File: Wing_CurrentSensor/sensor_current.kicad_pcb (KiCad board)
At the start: 2 copper layers, 50 x 50 mm, 18 parts, among them U1 TL084

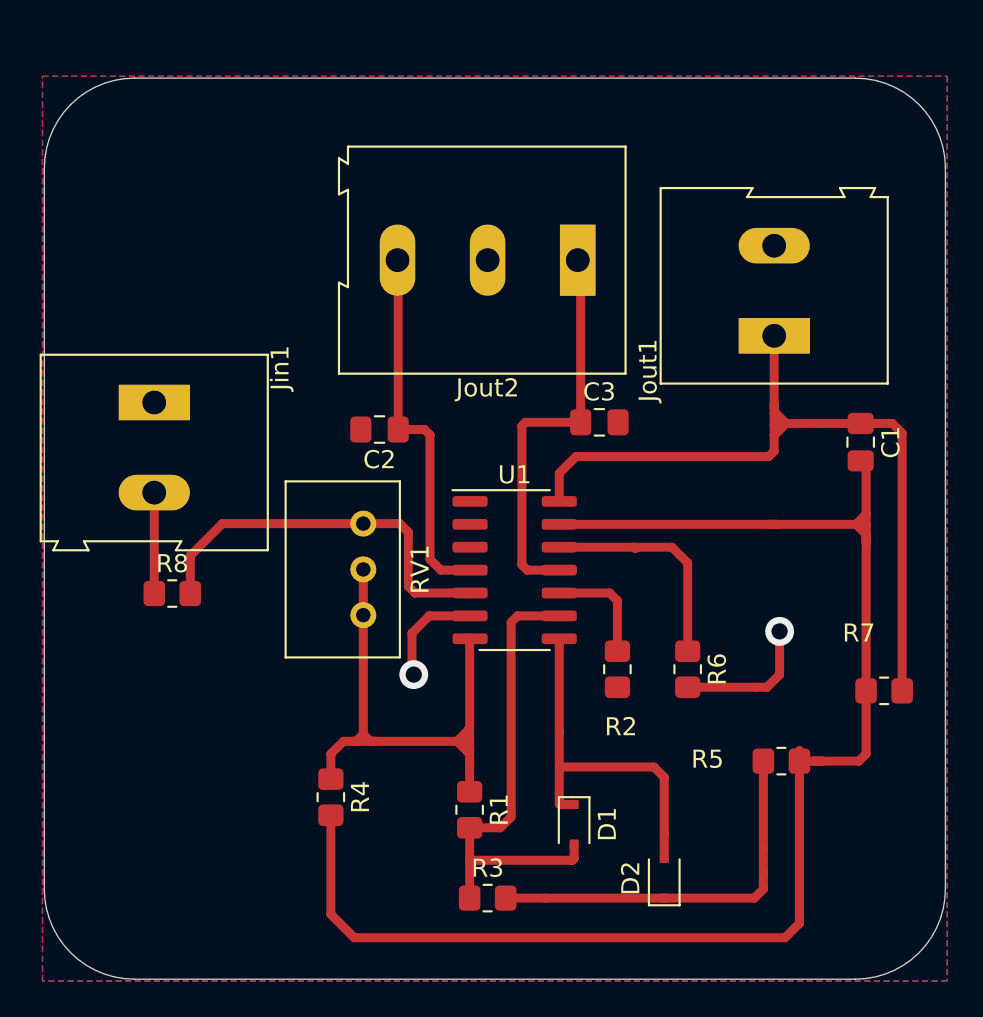
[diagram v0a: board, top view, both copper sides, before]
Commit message: Manual version
1rst version of the PCB ad8226 and TL084
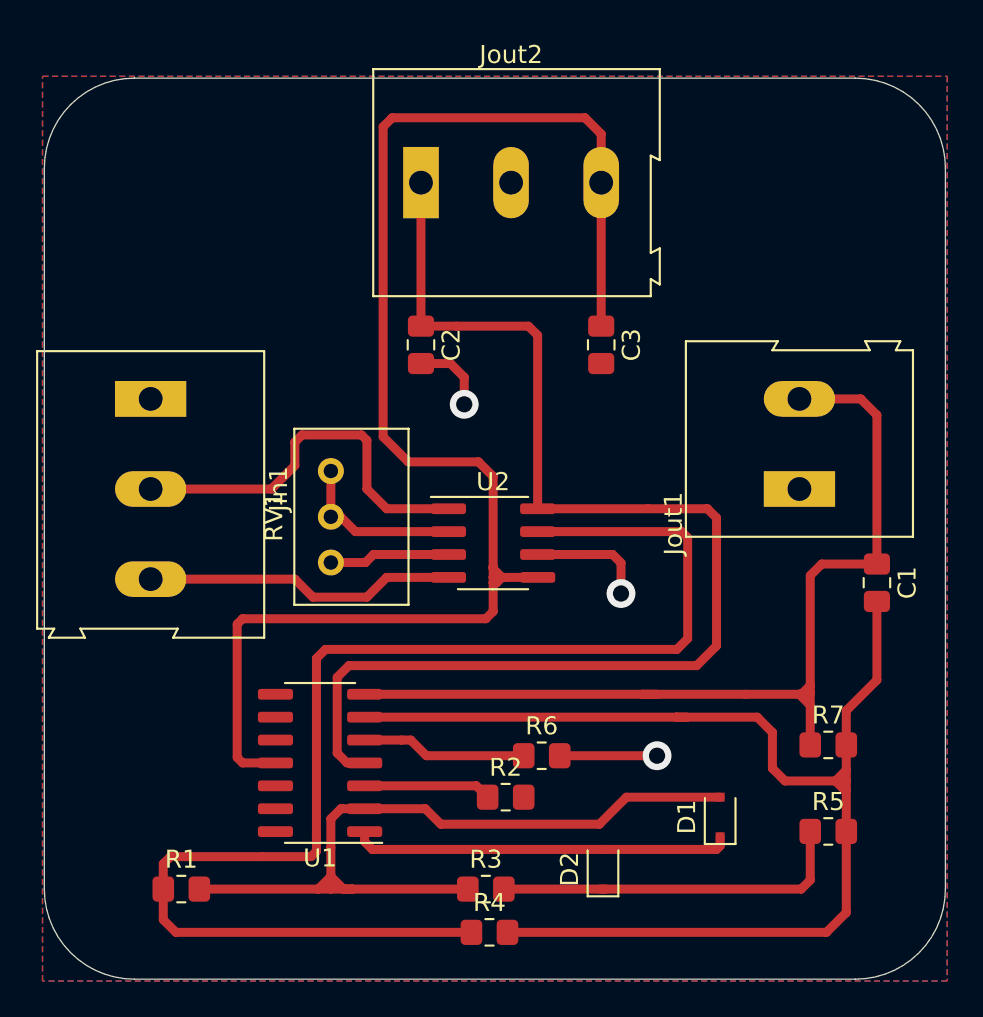
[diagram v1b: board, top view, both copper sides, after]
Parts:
- removed R8: 1K, Resistor_SMD:R_0805_2012Metric_Pad1.20x1.40mm_HandSolder
- added U2: AD8226, Package_SO:SOIC-8_3.9x4.9mm_P1.27mm, F.Cu at (65.9, 105.8)
- Jin1: value Screw_Terminal_01x02 -> Screw_Terminal_01x03; footprint TerminalBlock:TerminalBlock_Altech_AK300-2_P5.00mm -> TerminalBlock:TerminalBlock_Altech_AK300-3_P5.00mm
- moved R1 16.6 mm to (48.6, 125.0), turned to 0 degrees
- moved U1 15.2 mm to (56.3, 118.0), turned to 180 degrees
- moved R4 11.6 mm to (65.7, 127.4), turned to 0 degrees
- moved Jout2 9.70 mm to (61.9, 85.8), turned to 0 degrees
- moved R2 9.43 mm to (66.6, 119.9), turned to 0 degrees
- moved R6 9.42 mm to (68.6, 117.6), turned to 0 degrees
- moved Jout1 8.61 mm to (82.9, 102.8)
- moved RV1 8.20 mm to (56.9, 101.8), turned to 90 degrees
- moved D1 8.11 mm to (78.5, 121.0), turned to 90 degrees
- moved C1 7.85 mm to (87.2, 108.0)
- moved C2 5.23 mm to (61.9, 94.8), turned to 270 degrees
- moved R5 4.69 mm to (84.5, 121.8)
- moved R7 4.31 mm to (84.5, 117.0), turned to 0 degrees
- moved C3 4.30 mm to (71.9, 94.8), turned to 270 degrees
- moved D2 3.44 mm to (72.0, 123.9)
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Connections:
- Jin1 pad 2: /in+ -> /in-
- Jout1 pad 1: /OUT -> GND
- Jout1 pad 2: GND -> /OUT
- Jout2 pad 1: /-Vs -> /+Vs
- Jout2 pad 3: /+Vs -> /-Vs
- RV1 pad 1: /out1 -> Net-(RV1-Pad1)
- RV1 pad 2: /out1 -> Net-(RV1-Pad1)
- RV1 pad 3: Net-(R8-Pad2) -> Net-(RV1-Pad3)
- U1 pad 1: (no net) -> Net-(D1-Pad1)
- U1 pad 10: Net-(R2-Pad1) -> (no net)
- U1 pad 12: Net-(R6-Pad1) -> (no net)
- U1 pad 13: Net-(C1-Pad2) -> (no net)
- U1 pad 14: /OUT -> (no net)
- U1 pad 2: (no net) -> Net-(D1-Pad2)
- U1 pad 3: (no net) -> Net-(R2-Pad1)
- U1 pad 5: Net-(R8-Pad2) -> Net-(R6-Pad1)
- U1 pad 6: GND -> Net-(C1-Pad2)
- U1 pad 7: /out1 -> /OUT
- U1 pad 8: Net-(D1-Pad1) -> (no net)
- U1 pad 9: Net-(D1-Pad2) -> (no net)
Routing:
- net /-Vs: track 22.4 -> 83.1 mm
- net /+Vs: track 20.8 -> 69.2 mm
- net /out1: track 32.3 -> 75.4 mm
- net /in-: track 0.00 -> 21.8 mm
- net Net-(R8-Pad2): track 21.8 -> 0.00 mm
- net Net-(D1-Pad2): track 26.7 -> 44.1 mm
- net Net-(C1-Pad2): track 82.3 -> 68.8 mm
- net /in+: track 5.60 -> 17.4 mm
- net Net-(RV1-Pad1): track 0.00 -> 9.41 mm
- net /OUT: track 44.2 -> 53.6 mm
- net Net-(RV1-Pad3): track 0.00 -> 6.71 mm
- net GND: track 13.8 -> 18.9 mm, vias 2 -> 3
- net Net-(R6-Pad1): track 12.5 -> 9.19 mm
- net Net-(D2-Pad1): track 21.6 -> 19.9 mm
- net Net-(R2-Pad1): track 6.25 -> 7.09 mm

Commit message: update files
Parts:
- removed C3: 0.1μ, Capacitor_SMD:C_0805_2012Metric_Pad1.18x1.45mm_HandSolder
- removed Jin1, Jout2: Screw_Terminal_01x03, TerminalBlock:TerminalBlock_Altech_AK300-3_P5.00mm
- removed Jout1: Screw_Terminal_01x02, TerminalBlock:TerminalBlock_Altech_AK300-2_P5.00mm
- added J1: feather long, Connector_PinHeader_2.54mm:PinHeader_1x16_P2.54mm_Vertical, B.Cu at (152.4, 112.0)
- added J2: feather short, Connector_PinHeader_2.54mm:PinHeader_1x12_P2.54mm_Vertical, B.Cu at (152.4, 91.7)
- added J3: SJ-3524-SMT, CUI_SJ-3524-SMT, F.Cu at (110.8, 101.5)
- added R8: 10K, Resistor_SMD:R_0805_2012Metric_Pad1.20x1.40mm_HandSolder, F.Cu at (133.6, 104.7)
- added R9: 10K, Resistor_SMD:R_0805_2012Metric_Pad1.20x1.40mm_HandSolder, F.Cu at (137.8, 106.1)
- added REF**: MountingHole_2.7mm_M2.5, MountingHole:MountingHole_2.7mm_M2.5, F.Cu at (156.3, 92.9)
- added REF**: MountingHole_2.7mm_M2.5, MountingHole:MountingHole_2.7mm_M2.5, F.Cu at (156.3, 110.7)
- added REF**: MountingHole_2.7mm_M2.5, MountingHole:MountingHole_2.7mm_M2.5, F.Cu at (110.5, 110.7)
- added REF**: MountingHole_2.7mm_M2.5, MountingHole:MountingHole_2.7mm_M2.5, F.Cu at (110.5, 92.9)
- moved R1 106.4 mm to (153.3, 106.5), turned to 90 degrees
- moved R4 95.3 mm to (157.4, 101.3), turned to 90 degrees
- moved R3 90.8 mm to (153.3, 102.0), turned to 90 degrees
- moved U1 89.3 mm to (143.9, 100.7)
- moved R2 83.6 mm to (149.5, 109.0), turned to 180 degrees
- moved D2 81.0 mm to (150.2, 102.9), turned to 180 degrees
- moved R6 77.2 mm to (145.3, 109.0)
- moved D1 73.4 mm to (150.2, 105.5), turned to 0 degrees
- moved R5 73.0 mm to (153.3, 97.5), turned to 90 degrees
- moved C2 72.1 mm to (134.0, 94.8), turned to 0 degrees
- moved R7 70.4 mm to (151.2, 94.3)
- moved RV1 70.2 mm to (127.0, 97.9)
- moved U2 69.8 mm to (135.5, 100.5)
- moved C1 60.7 mm to (146.4, 94.7), turned to 0 degrees
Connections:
- net /+Vs renamed /VBUS
- R2 pad 2: GND -> /Vref
- R6 pad 2: GND -> /Vref
- U1 pad 11: /-Vs -> GND
- U1 pad 12: (no net) -> Net-(R8-Pad2)
- U1 pad 13: (no net) -> /Vref
- U1 pad 14: (no net) -> /Vref
- U2 pad 5: /-Vs -> GND
- U2 pad 6: GND -> /Vref
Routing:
- net /-Vs: track 83.1 -> 0.00 mm
- net Net-(C1-Pad2): track 68.8 -> 24.8 mm
- net /out1: track 75.4 -> 37.5 mm
- net /VBUS: track 69.2 -> 40.8 mm
- net Net-(D1-Pad2): track 44.1 -> 15.7 mm
- net GND: track 18.9 -> 42.9 mm
- net /Vref: track 0.00 -> 16.4 mm, vias 0 -> 2
- net Net-(D1-Pad1): track 21.0 -> 5.61 mm
- net Net-(R8-Pad2): track 0.00 -> 15.2 mm
- net Net-(D2-Pad1): track 19.9 -> 6.29 mm
- net Net-(R6-Pad1): track 9.19 -> 18.6 mm, vias 0 -> 2
- net Net-(R2-Pad1): track 7.09 -> 16.2 mm, vias 0 -> 2
- net /OUT: track 53.6 -> 45.3 mm, vias 0 -> 7
- net /in+: track 17.4 -> 15.7 mm
- net /in-: track 21.8 -> 23.1 mm
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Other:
- board size 50 x 50 mm -> 50.8 x 22.9 mm
- net class Default: clearance 0.3 -> 0.2; trace_width 0.5 -> 0.25
- net class vcc removed
- rule pad_to_mask_clearance: 0 -> 0.051
- rule trace_clearance: 0.3 -> 0.2
- board text added: "3V3"
- board text added: "A0"
- board text added: "A1"
- board text added: "A2"
- board text added: "A3"
- board text added: "A4"
- board text added: "A5"
- board text added: "AREF"
- board text added: "EN"
- board text added: "F0"
- board text added: "F1"
- board text added: "F2"
- board text added: "F3"
- board text added: "F4"
- board text added: "F5"
- board text added: "F6"
- board text added: "FREE"
- board text added: "GND"
- board text added: "MISO"
- board text added: "MOSI"
- board text added: "RX"
- board text added: "SCK"
- board text added: "SCL"
- board text added: "SDA"
- board text added: "TX"
- board text added: "VBAT"
- board text added: "VUSB"
- board text added: "~RST"

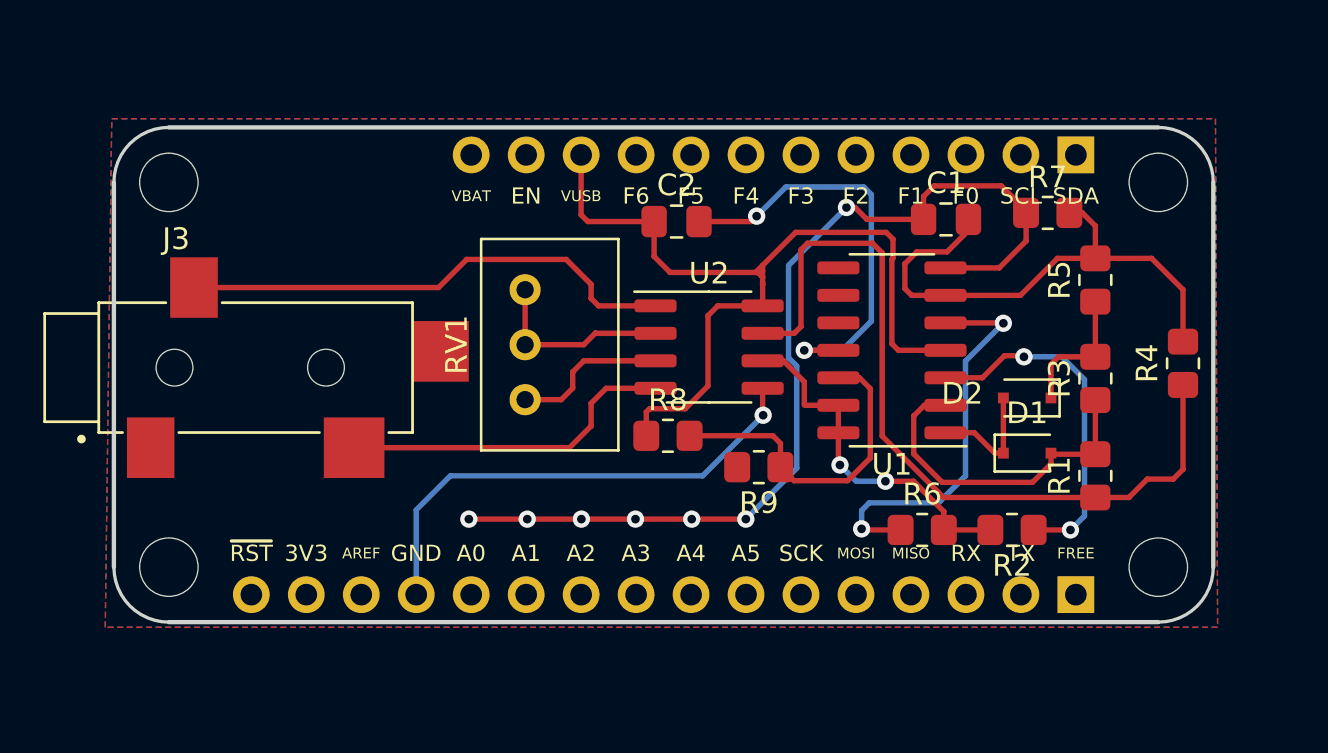
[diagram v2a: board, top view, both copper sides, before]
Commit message: Jack swapped and  update of labels
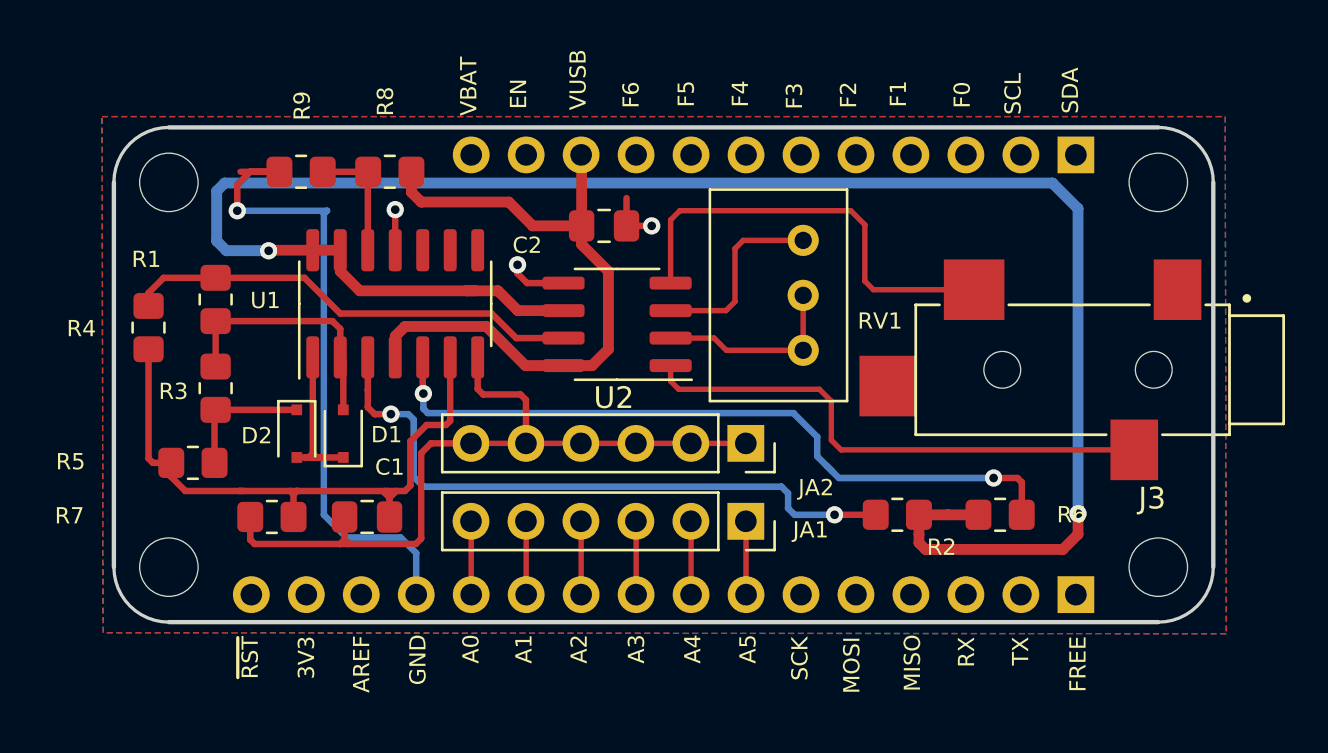
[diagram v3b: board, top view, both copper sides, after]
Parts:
- added JA1: Conn_01x06, Connector_PinSocket_2.54mm:PinSocket_1x06_P2.54mm_Vertical, F.Cu at (137.2, 108.6)
- added JA2: Conn_01x06, Connector_PinSocket_2.54mm:PinSocket_1x06_P2.54mm_Vertical, F.Cu at (137.2, 105.0)
- moved R4 47.8 mm to (109.6, 99.7), turned to 270 degrees
- moved J3 45.3 mm to (156.1, 101.6), turned to 180 degrees
- moved R5 42.5 mm to (111.7, 105.9), turned to 180 degrees
- moved R1 41.5 mm to (112.7, 98.3), turned to 270 degrees
- moved R3 40.7 mm to (112.7, 102.5), turned to 270 degrees
- moved R7 38.5 mm to (115.3, 108.4)
- moved D2 33.8 mm to (116.5, 104.5), turned to 270 degrees
- moved D1 31.6 mm to (118.6, 104.5), turned to 90 degrees
- moved C1 30.1 mm to (119.7, 108.4)
- moved R9 25.2 mm to (116.7, 92.5)
- moved U1 23.1 mm to (121.0, 98.5), turned to 90 degrees
- moved R8 17.7 mm to (120.8, 92.5), turned to 180 degrees
- moved RV1 13.2 mm to (139.8, 100.7), turned to 270 degrees
- moved R2 5.35 mm to (144.2, 108.3), turned to 0 degrees
- moved U2 4.38 mm to (131.2, 99.5), turned to 180 degrees
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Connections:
- net /Vref renamed /VREF
- net /in+ renamed /IN+
- net /in- renamed /IN-
- net /out1 renamed /OUT1
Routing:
- net /VREF: track 16.4 -> 88.0 mm
- net /OUT1: track 37.5 -> 21.2 mm
- net Net-(R6-Pad1): track 18.6 -> 33.9 mm
- net Net-(R2-Pad1): track 16.2 -> 29.8 mm
- net /VBUS: track 40.8 -> 31.0 mm
- net /OUT: track 45.3 -> 35.8 mm, vias 7 -> 0
- net Net-(R8-Pad2): track 15.2 -> 5.73 mm
- net GND: track 42.9 -> 37.4 mm, vias 3 -> 4
- net /IN+: track 15.7 -> 20.2 mm
- net Net-(C1-Pad2): track 24.8 -> 29.3 mm
- net Net-(D1-Pad2): track 15.7 -> 11.8 mm
- net /A5: track 0.00 -> 3.39 mm
- net /A0: track 0.00 -> 3.39 mm
- net /A4: track 0.00 -> 3.39 mm
- net /A3: track 0.00 -> 3.39 mm
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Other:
- net class Default: trace_width 0.25 -> 0.3
- net class Voltaje added: clearance 0.2, trace_width 0.5, via_dia 0.8, via_drill 0.4

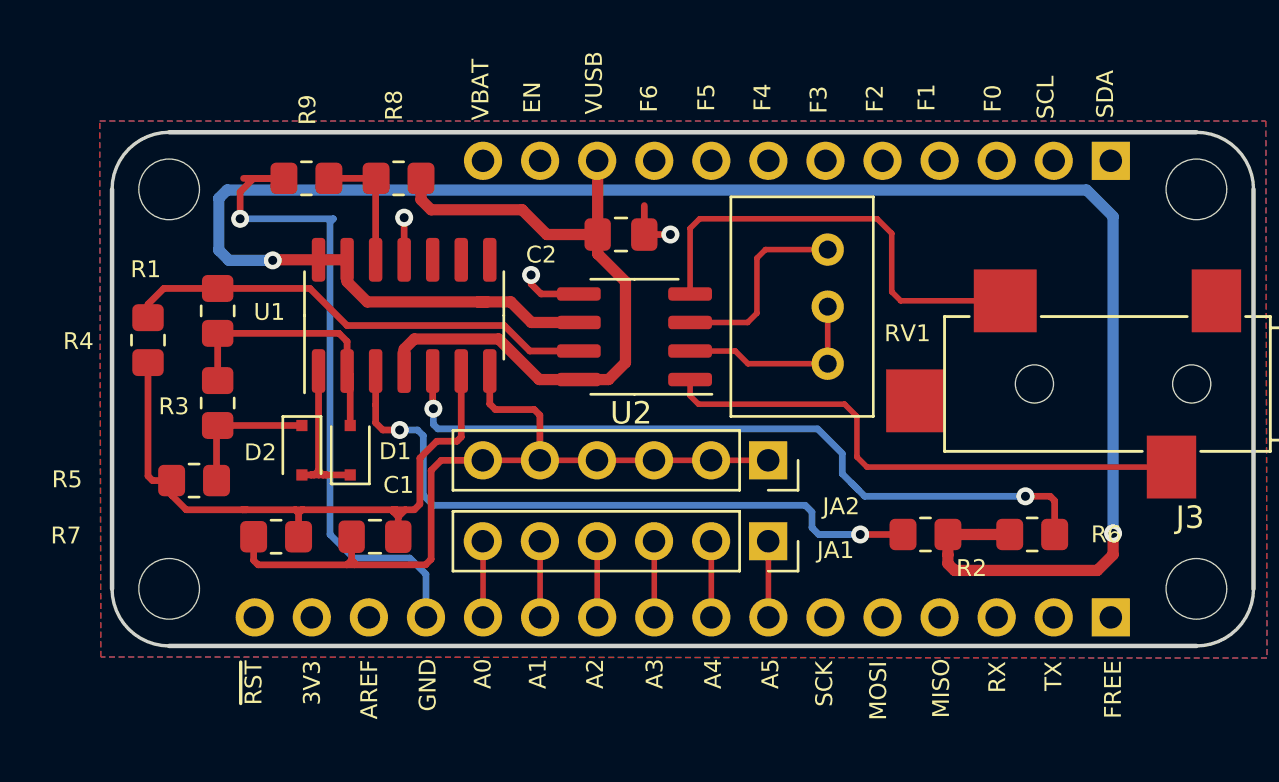
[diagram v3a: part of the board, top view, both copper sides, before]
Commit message: power at 3.3v and labels update
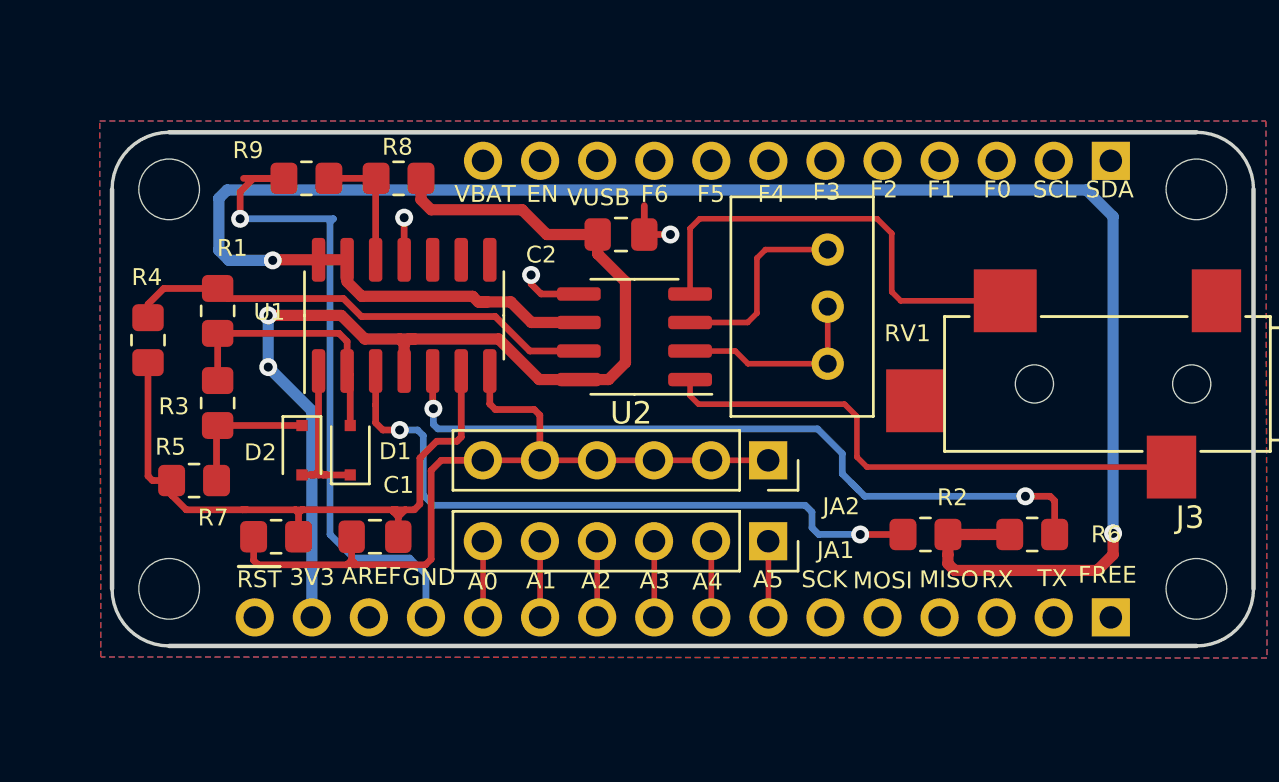
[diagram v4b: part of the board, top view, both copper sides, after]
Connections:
- C2 pad 1: /VBUS -> +3V3
- R8 pad 1: /VBUS -> +3V3
- U1 pad 4: /VBUS -> +3V3
- U2 pad 8: /VBUS -> +3V3
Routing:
- net +3V3: track 0.00 -> 59.0 mm, vias 0 -> 2
- net /VBUS: track 31.0 -> 0.05 mm
